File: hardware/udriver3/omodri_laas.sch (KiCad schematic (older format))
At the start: 12 parts, among them J1 Conn_01x11, J2 Conn_01x05, J3 Conn_01x03, J4 Conn_01x03

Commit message: Update of the schematics. Switches on GPIO72 & GPIO84 are missing. J1, J2 & J14 must be merged and connector placement optimized. TCXO must be changed from 20MHz to 25MHz for EtherCAT compatibility. PCB is partially routed in 6-Layers (mainly power supplies and and transistors). 8-Layers will be necessary.
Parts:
- added H1, H2, H3, H4: MountingHole, MountingHole:MountingHole_2.2mm_M2, symbol Mechanical:MountingHole
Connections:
- net sheet5F597565/ANALOG_IN1 renamed OMODRI_GPIO/ANALOG_IN1
- net sheet5F597565/ANALOG_IN2 renamed OMODRI_GPIO/ANALOG_IN2
- net sheet5F597565/COM_SPI_CLK renamed OMODRI_GPIO/COM_SPI_SOMI
- net sheet5F597565/COM_SPI_SIMO renamed OMODRI_GPIO/COM_SPI_SIMO
- net sheet5F597565/COM_SPI_SOMI renamed OMODRI_GPIO/~COM_SPI_CSn~
- net sheet5F597565/GPIO0 renamed OMODRI_GPIO/GPIO4
- net sheet5F597565/GPIO1 renamed OMODRI_GPIO/GPIO3
- net sheet5F597565/GPIO2 renamed OMODRI_GPIO/GPIO2
- net sheet5F597565/GPIO3 renamed OMODRI_GPIO/GPIO1
- net sheet5F597565/GPIO4 renamed OMODRI_GPIO/GPIO0
- net sheet5F597565/SPI_CLK renamed OMODRI_GPIO/SPI_SOMI
- net sheet5F597565/SPI_SIMO renamed OMODRI_GPIO/SPI_SIMO
- net sheet5F597565/SPI_SOMI renamed OMODRI_GPIO/~SPI_CSn~
- net sheet5F597565/~COM_SPI_CSn~ renamed OMODRI_GPIO/COM_SPI_CLK
- net sheet5F597565/~SPI_CSn~ renamed OMODRI_GPIO/SPI_CLK

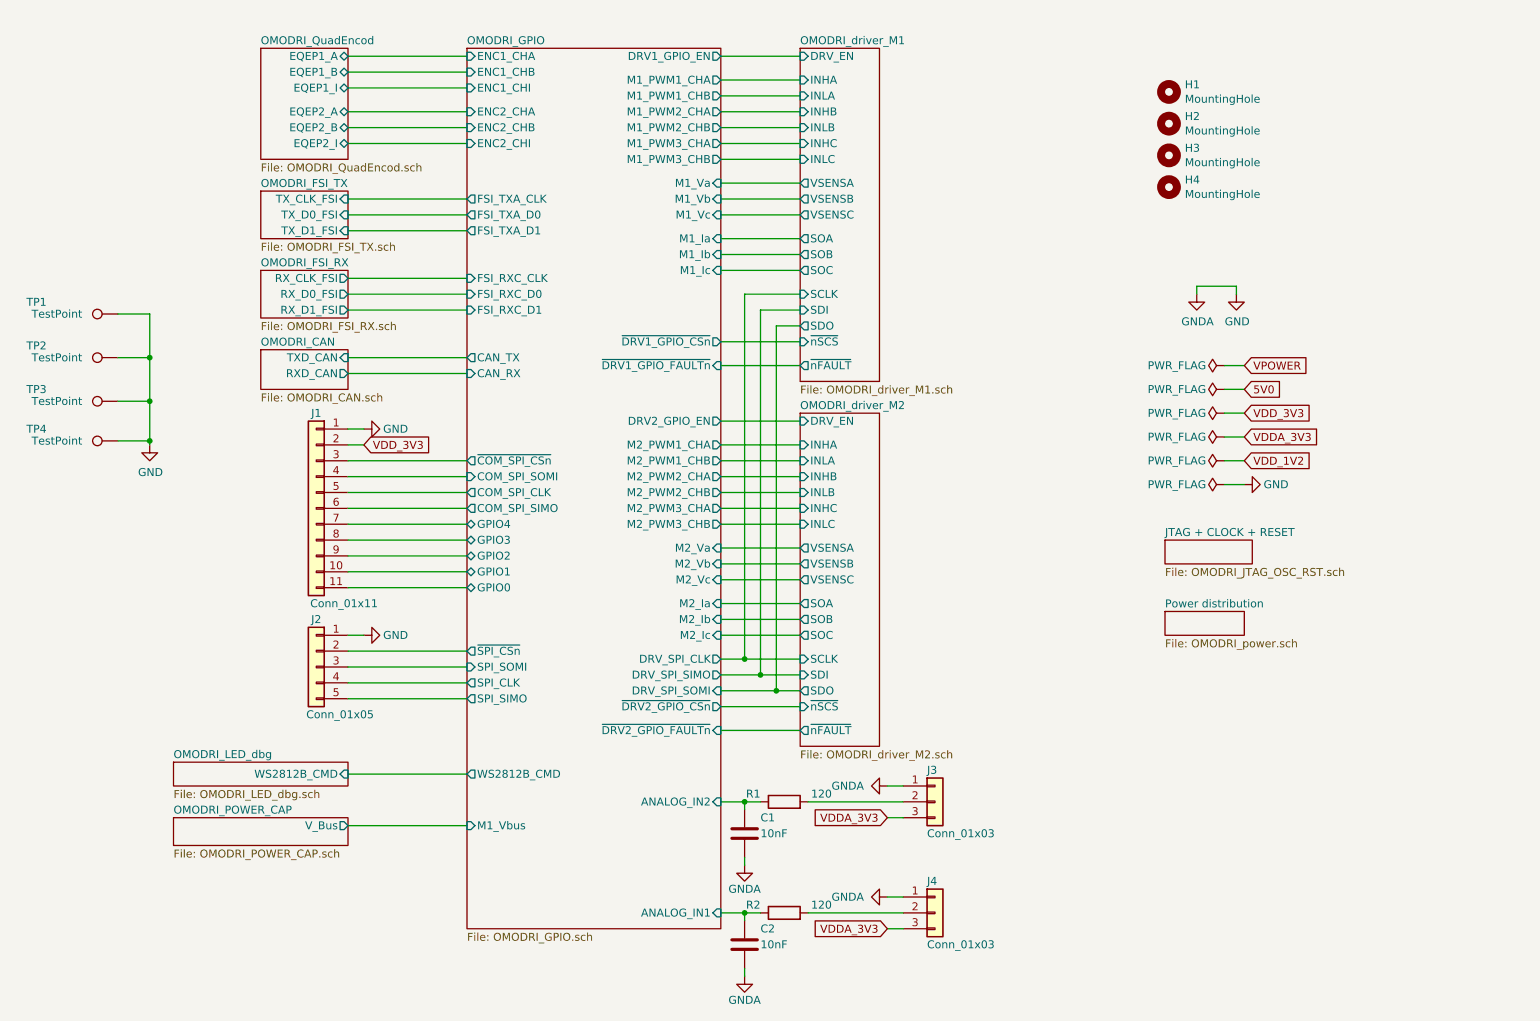
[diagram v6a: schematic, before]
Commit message: First release of the fully routed OMODRI PCB from LAAS. (8 layers)
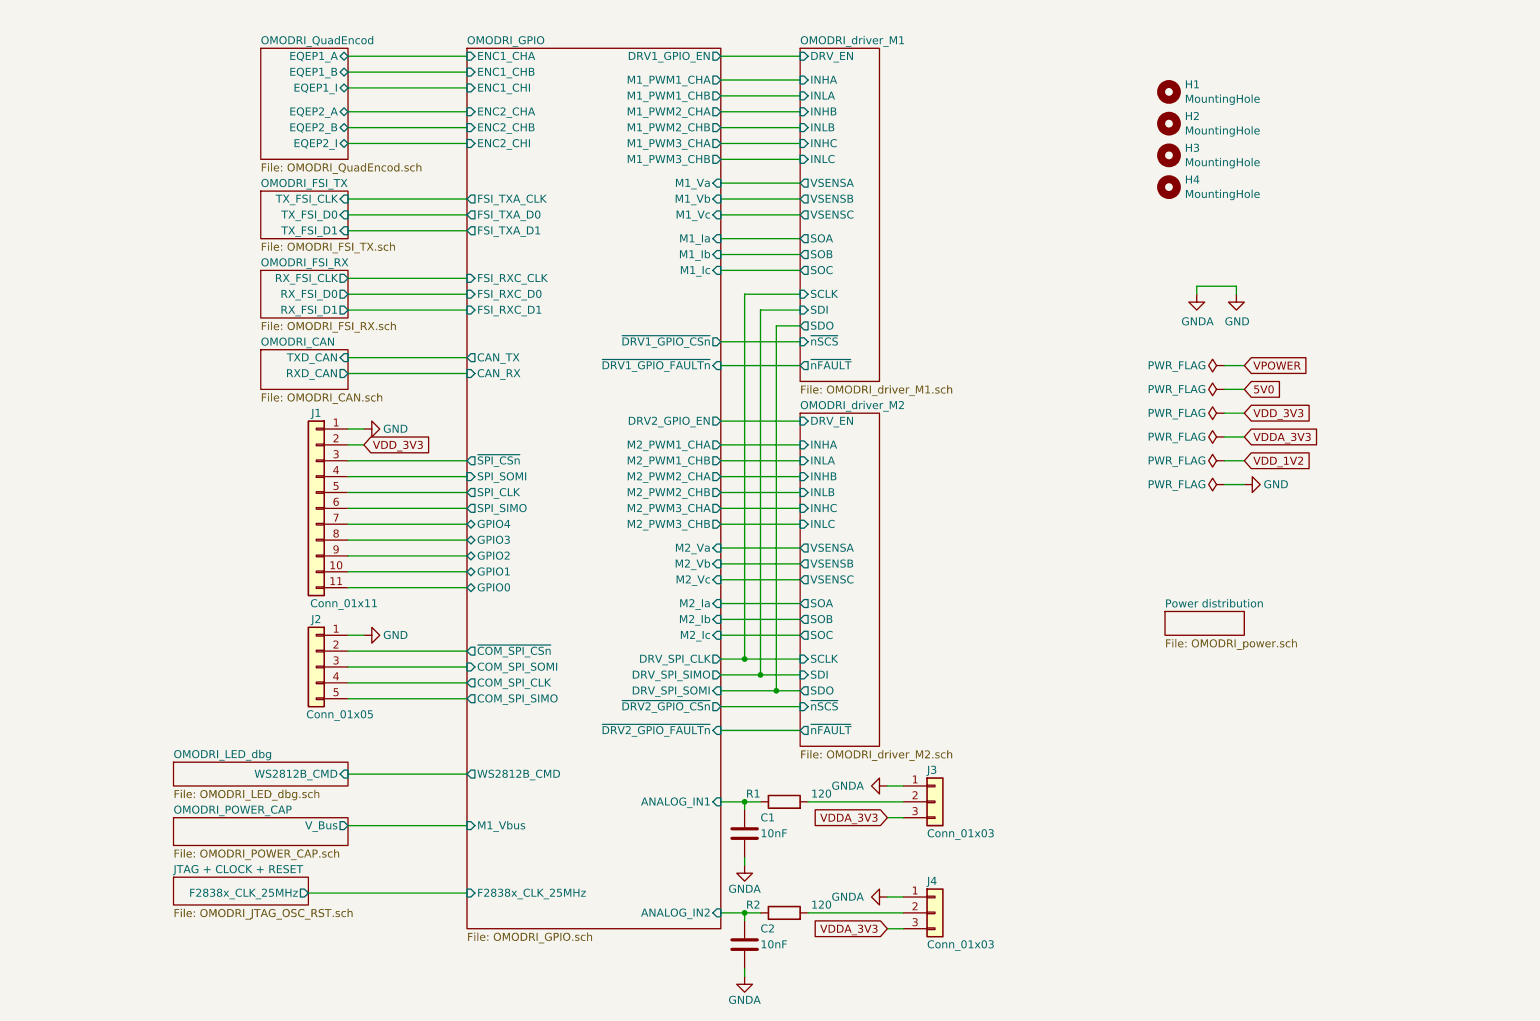
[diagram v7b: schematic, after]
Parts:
- removed TP1, TP2, TP3, TP4: TestPoint, TestPoint:TestPoint_Pad_D1.0mm, symbol Connector:TestPoint
- J1: footprint Connector_Hirose:Hirose_DF13-11P-1.25DSA_1x11_P1.25mm_Vertical -> udriver3:Hirose_DF13-11P-1.25DSA_1x11_P1.25mm_Vertical
- J2: footprint Connector_Hirose:Hirose_DF13-05P-1.25DSA_1x05_P1.25mm_Vertical -> udriver3:Hirose_DF13-05P-1.25DSA_1x05_P1.25mm_Vertical
- J3, J4: footprint Connector_Hirose:Hirose_DF13-03P-1.25DSA_1x03_P1.25mm_Vertical -> udriver3:Hirose_DF13-03P-1.25DSA_1x03_P1.25mm_Vertical
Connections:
- net OMODRI_GPIO/ANALOG_IN1: now also C1.1, R1.1; no longer C2.1, R2.1
- net OMODRI_GPIO/ANALOG_IN2: now also C2.1, R2.1; no longer C1.1, R1.1
- net OMODRI_GPIO/COM_SPI_CLK: now also J2.4 (Pin_4); no longer J1.5 (Pin_5)
- net OMODRI_GPIO/COM_SPI_SIMO: now also J2.5 (Pin_5); no longer J1.6 (Pin_6)
- net OMODRI_GPIO/COM_SPI_SOMI: now also J2.3 (Pin_3); no longer J1.4 (Pin_4)
- net OMODRI_GPIO/SPI_CLK: now also J1.5 (Pin_5); no longer J2.4 (Pin_4)
- net OMODRI_GPIO/SPI_SIMO: now also J1.6 (Pin_6); no longer J2.5 (Pin_5)
- net OMODRI_GPIO/SPI_SOMI: now also J1.4 (Pin_4); no longer J2.3 (Pin_3)
- net OMODRI_GPIO/~COM_SPI_CSn~: now also J2.2 (Pin_2); no longer J1.3 (Pin_3)
- net OMODRI_GPIO/~SPI_CSn~: now also J1.3 (Pin_3); no longer J2.2 (Pin_2)
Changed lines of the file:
@@
 $Descr A4 11693 8268
 encoding utf-8
-Sheet 1 17
+Sheet 1 19
 Title "Open MOtor DRiver Initiative (OMODRI)"
 Date ""
@@
 F 0 "J3" H 6500 5700 50  0000 L CNN
 F 1 "Conn_01x03" H 6500 5300 50  0000 L CNN
-F 2 "Connector_Hirose:Hirose_DF13-03P-1.25DSA_1x03_P1.25mm_Vertical" H 6550 5500 50  0001 C CNN
+F 2 "udriver3:Hirose_DF13-03P-1.25DSA_1x03_P1.25mm_Vertical" H 6550 5500 50  0001 C CNN
 F 3 "https://www.hirose.com/product/document?clcode=&productname=&series=DF13&documenttype=Catalog&lang=en&documentid=D31687_en" H 6550 5500 50  0001 C CNN
 F 4 "DF13-3P-1.25DSA(75)-ND" H 6550 5500 50  0001 C CNN "DigiKey"
@@
 F 0 "J1" H 2650 4250 50  0000 C CNN
 F 1 "Conn_01x11" H 2475 3050 50  0000 C CNN
-F 2 "Connector_Hirose:Hirose_DF13-11P-1.25DSA_1x11_P1.25mm_Vertical" H 2650 3650 50  0001 C CNN
+F 2 "udriver3:Hirose_DF13-11P-1.25DSA_1x11_P1.25mm_Vertical" H 2650 3650 50  0001 C CNN
 F 3 "https://www.hirose.com/product/document?clcode=&productname=&series=DF13&documenttype=Catalog&lang=en&documentid=D31687_en" H 2650 3650 50  0001 C CNN
 F 4 "H126373-ND" H 2650 3650 50  0001 C CNN "DigiKey"
@@
 F 0 "J2" H 2650 4950 50  0000 C CNN
 F 1 "Conn_01x05" H 2500 4350 50  0000 C CNN
-F 2 "Connector_Hirose:Hirose_DF13-05P-1.25DSA_1x05_P1.25mm_Vertical" H 2650 4650 50  0001 C CNN
+F 2 "udriver3:Hirose_DF13-05P-1.25DSA_1x05_P1.25mm_Vertical" H 2650 4650 50  0001 C CNN
 F 3 "https://www.hirose.com/product/document?clcode=&productname=&series=DF13&documenttype=Catalog&lang=en&documentid=D31687_en" H 2650 4650 50  0001 C CNN
 F 4 "DF13-5P-1.25DSA(75)-ND" H 2650 4650 50  0001 C CNN "DigiKey"
@@
 $EndSheet
 $Sheet
-S 2300 2150 550  300
-U 5F5B5760
-F0 "OMODRI_FSI_RX" 50
-F1 "OMODRI_FSI_RX.sch" 50
-F2 "RX_D0_FSI" O R 2850 2300 50
-F3 "RX_D1_FSI" O R 2850 2400 50
-F4 "RX_CLK_FSI" O R 2850 2200 50
-$EndSheet
-$Sheet
-S 8000 3850 550  150
-U 5F5CAA29
-F0 "JTAG + CLOCK + RESET" 50
-F1 "OMODRI_JTAG_OSC_RST.sch" 50
-$EndSheet
-$Sheet
 S 2300 1650 550  300
 U 5F5DA2EB
 F0 "OMODRI_FSI_TX" 50
 F1 "OMODRI_FSI_TX.sch" 50
-F2 "TX_CLK_FSI" I R 2850 1700 50
-F3 "TX_D0_FSI" I R 2850 1800 50
-F4 "TX_D1_FSI" I R 2850 1900 50
+F2 "TX_FSI_CLK" I R 2850 1700 50
+F3 "TX_FSI_D0" I R 2850 1800 50
+F4 "TX_FSI_D1" I R 2850 1900 50
 $EndSheet
 Wire Wire Line
@@
 F 0 "J4" H 6500 6400 50  0000 L CNN
 F 1 "Conn_01x03" H 6500 6000 50  0000 L CNN
-F 2 "Connector_Hirose:Hirose_DF13-03P-1.25DSA_1x03_P1.25mm_Vertical" H 6550 6200 50  0001 C CNN
+F 2 "udriver3:Hirose_DF13-03P-1.25DSA_1x03_P1.25mm_Vertical" H 6550 6200 50  0001 C CNN
 F 3 "https://www.hirose.com/product/document?clcode=&productname=&series=DF13&documenttype=Catalog&lang=en&documentid=D31687_en" H 6550 6200 50  0001 C CNN
 F 4 "DF13-3P-1.25DSA(75)-ND" H 6550 6200 50  0001 C CNN "DigiKey"
@@
 Wire Wire Line
 	5350 5900 5350 5850
-$Comp
-L Connector:TestPoint TP?
-U 1 1 623BF9E4
-P 1400 2425
-AR Path="/5F310311/623BF9E4" Ref="TP?"  Part="1"
-AR Path="/5F3255E8/623BF9E4" Ref="TP?"  Part="1"
-AR Path="/5F387075/623BF9E4" Ref="TP?"  Part="1"
-AR Path="/623BF9E4" Ref="TP1"  Part="1"
-F 0 "TP1" V 1475 2875 50  0000 L CNN
-F 1 "TestPoint" V 1400 2650 50  0000 L CNN
-F 2 "TestPoint:TestPoint_Pad_D1.0mm" H 1600 2425 50  0001 C CNN
-F 3 "~" H 1600 2425 50  0001 C CNN
-	1    1400 2425
-	0    -1   -1   0
-$EndComp
-$Comp
-L power:GND #PWR?
-U 1 1 623C03FA
-P 1600 3250
-AR Path="/5F3A3F16/623C03FA" Ref="#PWR?"  Part="1"
-AR Path="/5F7A5BAE/623C03FA" Ref="#PWR?"  Part="1"
-AR Path="/5F68F8CB/623C03FA" Ref="#PWR?"  Part="1"
-AR Path="/5F4C38EC/623C03FA" Ref="#PWR?"  Part="1"
-AR Path="/623C03FA" Ref="#PWR04"  Part="1"
-F 0 "#PWR04" H 1600 3000 50  0001 C CNN
-F 1 "GND" H 1605 3077 50  0000 C CNN
-F 2 "" H 1600 3250 50  0001 C CNN
-F 3 "" H 1600 3250 50  0001 C CNN
-	1    1600 3250
-	1    0    0    -1
-$EndComp
-Wire Wire Line
-	1600 3225 1600 3250
-Wire Wire Line
-	1600 2975 1600 3225
-Connection ~ 1600 3225
-Wire Wire Line
-	1600 2700 1600 2975
-Connection ~ 1600 2975
-Wire Wire Line
-	1600 2425 1600 2700
-Connection ~ 1600 2700
-Wire Wire Line
-	1400 2425 1600 2425
-Wire Wire Line
-	1400 2700 1600 2700
-Wire Wire Line
-	1400 2975 1600 2975
-Wire Wire Line
-	1400 3225 1600 3225
-$Comp
-L Connector:TestPoint TP?
-U 1 1 624048CF
-P 1400 2700
-AR Path="/5F310311/624048CF" Ref="TP?"  Part="1"
-AR Path="/5F3255E8/624048CF" Ref="TP?"  Part="1"
-AR Path="/5F387075/624048CF" Ref="TP?"  Part="1"
-AR Path="/624048CF" Ref="TP2"  Part="1"
-F 0 "TP2" V 1475 3150 50  0000 L CNN
-F 1 "TestPoint" V 1400 2925 50  0000 L CNN
-F 2 "TestPoint:TestPoint_Pad_D1.0mm" H 1600 2700 50  0001 C CNN
-F 3 "~" H 1600 2700 50  0001 C CNN
-	1    1400 2700
-	0    -1   -1   0
-$EndComp
-$Comp
-L Connector:TestPoint TP?
-U 1 1 62404BE8
-P 1400 2975
-AR Path="/5F310311/62404BE8" Ref="TP?"  Part="1"
-AR Path="/5F3255E8/62404BE8" Ref="TP?"  Part="1"
-AR Path="/5F387075/62404BE8" Ref="TP?"  Part="1"
-AR Path="/62404BE8" Ref="TP3"  Part="1"
-F 0 "TP3" V 1475 3425 50  0000 L CNN
-F 1 "TestPoint" V 1400 3200 50  0000 L CNN
-F 2 "TestPoint:TestPoint_Pad_D1.0mm" H 1600 2975 50  0001 C CNN
-F 3 "~" H 1600 2975 50  0001 C CNN
-	1    1400 2975
-	0    -1   -1   0
-$EndComp
-$Comp
-L Connector:TestPoint TP?
-U 1 1 62404E47
-P 1400 3225
-AR Path="/5F310311/62404E47" Ref="TP?"  Part="1"
-AR Path="/5F3255E8/62404E47" Ref="TP?"  Part="1"
-AR Path="/5F387075/62404E47" Ref="TP?"  Part="1"
-AR Path="/62404E47" Ref="TP4"  Part="1"
-F 0 "TP4" V 1475 3675 50  0000 L CNN
-F 1 "TestPoint" V 1400 3450 50  0000 L CNN
-F 2 "TestPoint:TestPoint_Pad_D1.0mm" H 1600 3225 50  0001 C CNN
-F 3 "~" H 1600 3225 50  0001 C CNN
-	1    1400 3225
-	0    -1   -1   0
-$EndComp
 $Comp
 L power:PWR_FLAG #FLG01
@@
 F11 "DRV1_GPIO_EN" O R 5200 800 50
 F12 "DRV2_GPIO_EN" O R 5200 3100 50
-F13 "COM_SPI_SIMO" O L 3600 3650 50
-F14 "COM_SPI_SOMI" I L 3600 3450 50
-F15 "COM_SPI_CLK" O L 3600 3550 50
+F13 "COM_SPI_SIMO" O L 3600 4850 50
+F14 "COM_SPI_SOMI" I L 3600 4650 50
+F15 "COM_SPI_CLK" O L 3600 4750 50
 F16 "M1_PWM1_CHA" O R 5200 950 50
 F17 "M1_PWM1_CHB" O R 5200 1050 50
@@
 F48 "FSI_TXA_D0" O L 3600 1800 50
 F49 "FSI_TXA_D1" O L 3600 1900 50
-F50 "ANALOG_IN1" I R 5200 6200 50
-F51 "ANALOG_IN2" I R 5200 5500 50
-F52 "~COM_SPI_CSn~" O L 3600 3350 50
+F50 "ANALOG_IN1" I R 5200 5500 50
+F51 "ANALOG_IN2" I R 5200 6200 50
+F52 "~COM_SPI_CSn~" O L 3600 4550 50
 F53 "WS2812B_CMD" O L 3600 5325 50
 F54 "GPIO0" B L 3600 4150 50
@@
 F57 "GPIO3" B L 3600 3850 50
 F58 "GPIO4" B L 3600 3750 50
-F59 "SPI_SIMO" O L 3600 4850 50
-F60 "SPI_SOMI" I L 3600 4650 50
-F61 "SPI_CLK" O L 3600 4750 50
-F62 "~SPI_CSn~" O L 3600 4550 50
+F59 "SPI_SIMO" O L 3600 3650 50
+F60 "SPI_SOMI" I L 3600 3450 50
+F61 "SPI_CLK" O L 3600 3550 50
+F62 "~SPI_CSn~" O L 3600 3350 50
 F63 "FSI_RXC_CLK" I L 3600 2200 50
 F64 "FSI_RXC_D0" I L 3600 2300 50
 F65 "FSI_RXC_D1" I L 3600 2400 50
+F66 "F2838x_CLK_25MHz" I L 3600 6075 50
 $EndSheet
 $Comp
@@
 F7 "EQEP2_I" B R 2850 1350 50
 $EndSheet
+$Sheet
+S 1750 5975 850  175
+U 5F5CAA29
+F0 "JTAG + CLOCK + RESET" 50
+F1 "OMODRI_JTAG_OSC_RST.sch" 50
+F2 "F2838x_CLK_25MHz" O R 2600 6075 50
+$EndSheet
+Wire Wire Line
+	2600 6075 3600 6075
+$Sheet
+S 2300 2150 550  300
+U 5F5B5760
+F0 "OMODRI_FSI_RX" 50
+F1 "OMODRI_FSI_RX.sch" 50
+F2 "RX_FSI_D0" O R 2850 2300 50
+F3 "RX_FSI_D1" O R 2850 2400 50
+F4 "RX_FSI_CLK" O R 2850 2200 50
+$EndSheet
 $EndSCHEMATC

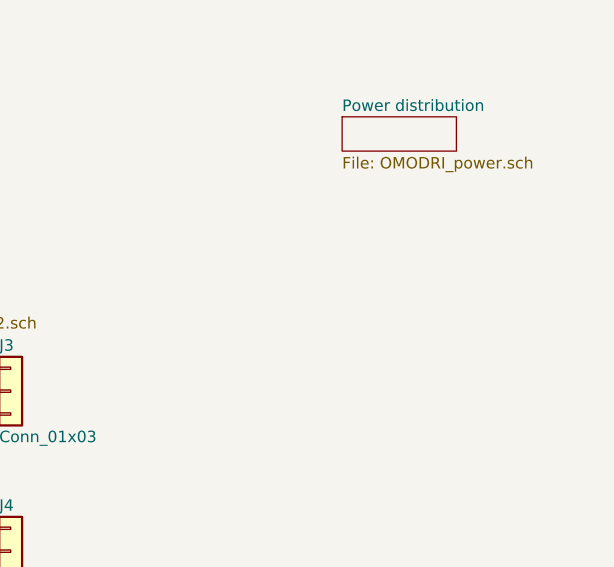
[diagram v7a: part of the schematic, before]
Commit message: Update of the µOmodri PCB with Gerber, stencil and assembly files.
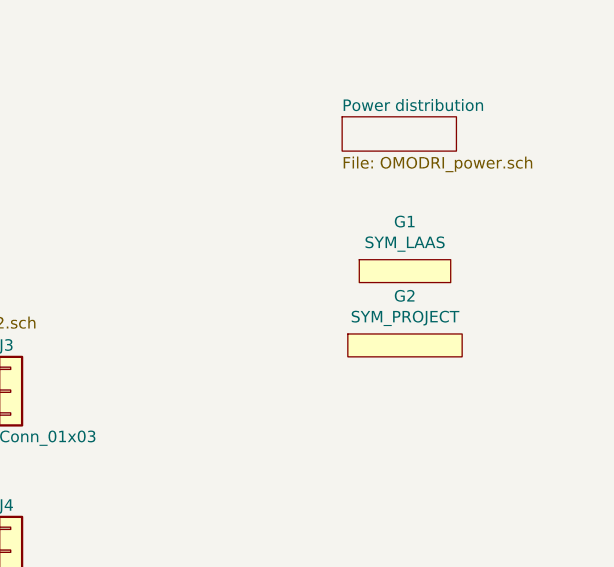
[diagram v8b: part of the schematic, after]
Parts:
- added G1: SYM_LAAS, udriver3:logo_laas, symbol omodri_lib:SYM_LAAS
- added G2: SYM_PROJECT, udriver3:logo_OpenHardware, symbol omodri_lib:SYM_PROJECT
- J1: DigiKey H126373-ND -> DF13-11P-1.25DSA-ND; Mouser 798-DF13-11P125DSA75 -> 798-DF13-11P-1.25DSA; Part No DF13-11P-1.25DSA(75) -> DF13-11P-1.25DSA; RS 188-6390 -> (none)
- J2: DigiKey DF13-5P-1.25DSA(75)-ND -> H2194-ND; Mouser 798-DF13-5P-125DSA75 -> 798-DF13-5P-1.25DSA; Part No DF13-5P-1.25DSA(75) -> DF13-5P-1.25DSA; RS 188-6358 -> 503-7912
- J3, J4: DigiKey DF13-3P-1.25DSA(75)-ND -> H2192-ND; Mouser 798-DF13-3P-125DSA75 -> 798-DF13-3P-1.25DSA; Part No DF13-3P-1.25DSA(75) -> DF13-3P-1.25DSA; RS 188-6281 -> 175-0666
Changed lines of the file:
@@
 F 2 "udriver3:Hirose_DF13-03P-1.25DSA_1x03_P1.25mm_Vertical" H 6550 5500 50  0001 C CNN
 F 3 "https://www.hirose.com/product/document?clcode=&productname=&series=DF13&documenttype=Catalog&lang=en&documentid=D31687_en" H 6550 5500 50  0001 C CNN
-F 4 "DF13-3P-1.25DSA(75)-ND" H 6550 5500 50  0001 C CNN "DigiKey"
+F 4 "H2192-ND" H 6550 5500 50  0001 C CNN "DigiKey"
 F 5 "2916340" H 6550 5500 50  0001 C CNN "Farnell"
-F 6 "798-DF13-3P-125DSA75" H 6550 5500 50  0001 C CNN "Mouser"
-F 7 "DF13-3P-1.25DSA(75)" H 6550 5500 50  0001 C CNN "Part No"
-F 8 "188-6281" H 6550 5500 50  0001 C CNN "RS"
+F 6 "798-DF13-3P-1.25DSA" H 6550 5500 50  0001 C CNN "Mouser"
+F 7 "DF13-3P-1.25DSA" H 6550 5500 50  0001 C CNN "Part No"
+F 8 "175-0666" H 6550 5500 50  0001 C CNN "RS"
 	1    6550 5500
 	1    0    0    -1
@@
 F 2 "udriver3:Hirose_DF13-11P-1.25DSA_1x11_P1.25mm_Vertical" H 2650 3650 50  0001 C CNN
 F 3 "https://www.hirose.com/product/document?clcode=&productname=&series=DF13&documenttype=Catalog&lang=en&documentid=D31687_en" H 2650 3650 50  0001 C CNN
-F 4 "H126373-ND" H 2650 3650 50  0001 C CNN "DigiKey"
-F 5 "798-DF13-11P125DSA75" H 2650 3650 50  0001 C CNN "Mouser"
-F 6 "DF13-11P-1.25DSA(75)" H 2650 3650 50  0001 C CNN "Part No"
-F 7 "188-6390" H 2650 3650 50  0001 C CNN "RS"
+F 4 "DF13-11P-1.25DSA-ND" H 2650 3650 50  0001 C CNN "DigiKey"
+F 5 "798-DF13-11P-1.25DSA" H 2650 3650 50  0001 C CNN "Mouser"
+F 6 "DF13-11P-1.25DSA" H 2650 3650 50  0001 C CNN "Part No"
+F 7 "" H 2650 3650 50  0001 C CNN "RS"
 	1    2650 3650
 	-1   0    0    -1
@@
 F 2 "udriver3:Hirose_DF13-05P-1.25DSA_1x05_P1.25mm_Vertical" H 2650 4650 50  0001 C CNN
 F 3 "https://www.hirose.com/product/document?clcode=&productname=&series=DF13&documenttype=Catalog&lang=en&documentid=D31687_en" H 2650 4650 50  0001 C CNN
-F 4 "DF13-5P-1.25DSA(75)-ND" H 2650 4650 50  0001 C CNN "DigiKey"
+F 4 "H2194-ND" H 2650 4650 50  0001 C CNN "DigiKey"
 F 5 "2427589" H 2650 4650 50  0001 C CNN "Farnell"
-F 6 "798-DF13-5P-125DSA75" H 2650 4650 50  0001 C CNN "Mouser"
-F 7 "DF13-5P-1.25DSA(75)" H 2650 4650 50  0001 C CNN "Part No"
-F 8 "188-6358" H 2650 4650 50  0001 C CNN "RS"
+F 6 "798-DF13-5P-1.25DSA" H 2650 4650 50  0001 C CNN "Mouser"
+F 7 "DF13-5P-1.25DSA" H 2650 4650 50  0001 C CNN "Part No"
+F 8 "503-7912" H 2650 4650 50  0001 C CNN "RS"
 	1    2650 4650
 	-1   0    0    -1
@@
 F 2 "udriver3:Hirose_DF13-03P-1.25DSA_1x03_P1.25mm_Vertical" H 6550 6200 50  0001 C CNN
 F 3 "https://www.hirose.com/product/document?clcode=&productname=&series=DF13&documenttype=Catalog&lang=en&documentid=D31687_en" H 6550 6200 50  0001 C CNN
-F 4 "DF13-3P-1.25DSA(75)-ND" H 6550 6200 50  0001 C CNN "DigiKey"
+F 4 "H2192-ND" H 6550 6200 50  0001 C CNN "DigiKey"
 F 5 "2916340" H 6550 6200 50  0001 C CNN "Farnell"
-F 6 "798-DF13-3P-125DSA75" H 6550 6200 50  0001 C CNN "Mouser"
-F 7 "DF13-3P-1.25DSA(75)" H 6550 6200 50  0001 C CNN "Part No"
-F 8 "188-6281" H 6550 6200 50  0001 C CNN "RS"
+F 6 "798-DF13-3P-1.25DSA" H 6550 6200 50  0001 C CNN "Mouser"
+F 7 "DF13-3P-1.25DSA" H 6550 6200 50  0001 C CNN "Part No"
+F 8 "175-0666" H 6550 6200 50  0001 C CNN "RS"
 	1    6550 6200
 	1    0    0    -1
@@
 F4 "RX_FSI_CLK" O R 2850 2200 50
 $EndSheet
+$Comp
+L omodri_lib:SYM_LAAS G1
+U 1 1 5FB102A1
+P 8275 4975
+F 0 "G1" H 8275 5190 50  0000 C CNN
+F 1 "SYM_LAAS" H 8275 5099 50  0000 C CNN
+F 2 "udriver3:logo_laas" H 8275 4975 50  0001 C CNN
+F 3 "" H 8275 4975 50  0001 C CNN
+	1    8275 4975
+	1    0    0    -1
+$EndComp
+$Comp
+L omodri_lib:SYM_PROJECT G2
+U 1 1 5FB10CDC
+P 8275 5300
+F 0 "G2" H 8275 5515 50  0000 C CNN
+F 1 "SYM_PROJECT" H 8275 5424 50  0000 C CNN
+F 2 "udriver3:logo_OpenHardware" H 8275 5300 50  0001 C CNN
+F 3 "" H 8275 5300 50  0001 C CNN
+	1    8275 5300
+	1    0    0    -1
+$EndComp
 $EndSCHEMATC
